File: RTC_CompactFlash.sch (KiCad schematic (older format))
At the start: 23 parts

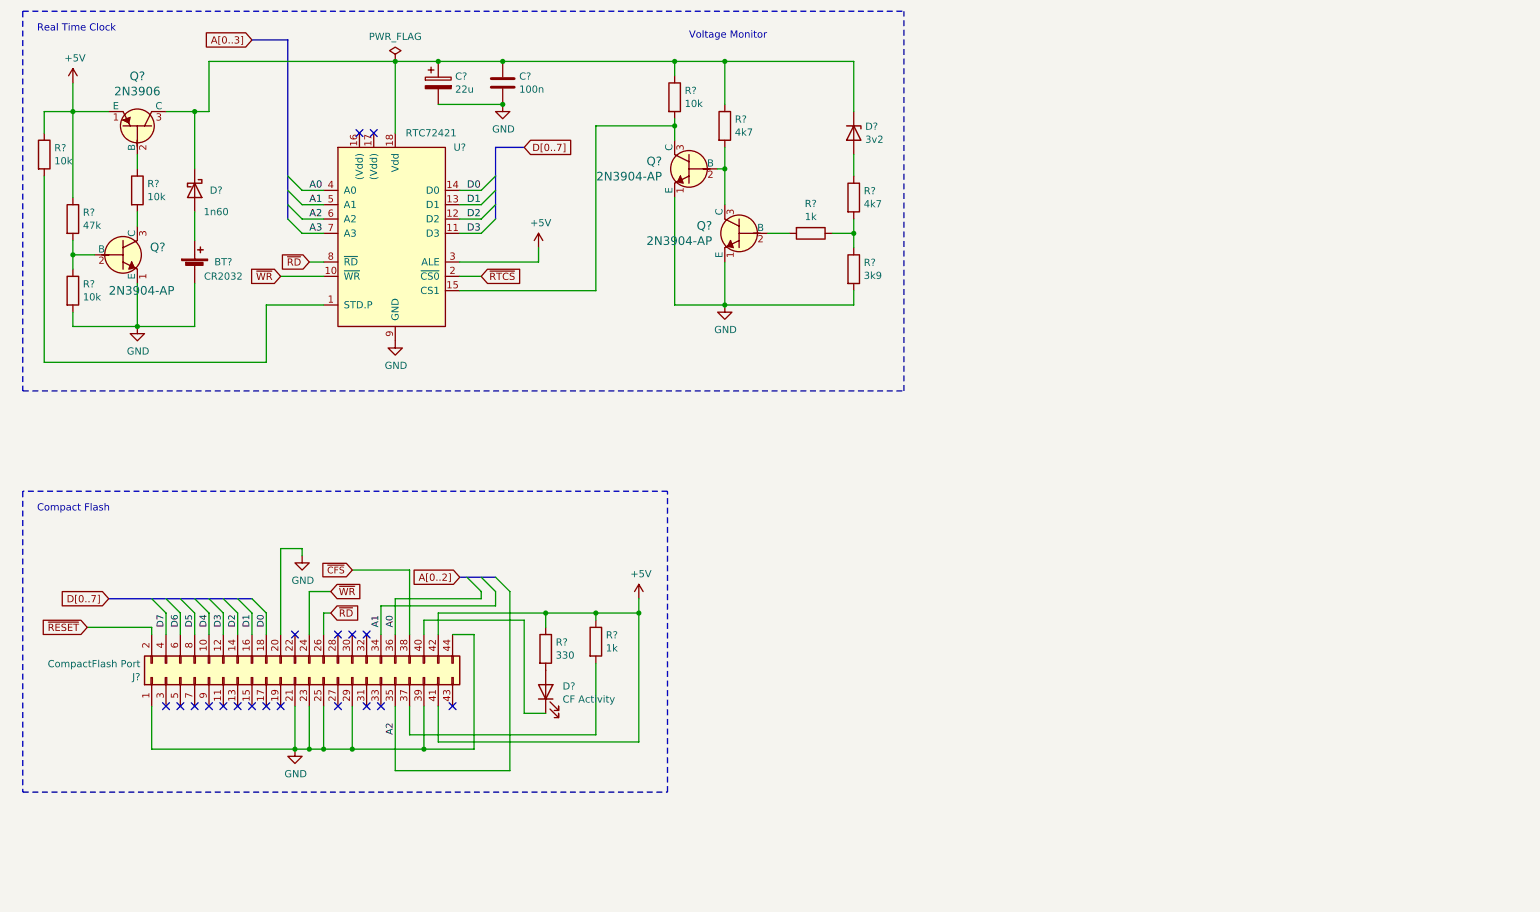
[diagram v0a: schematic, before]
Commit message: Added RTC voltage detection circuit
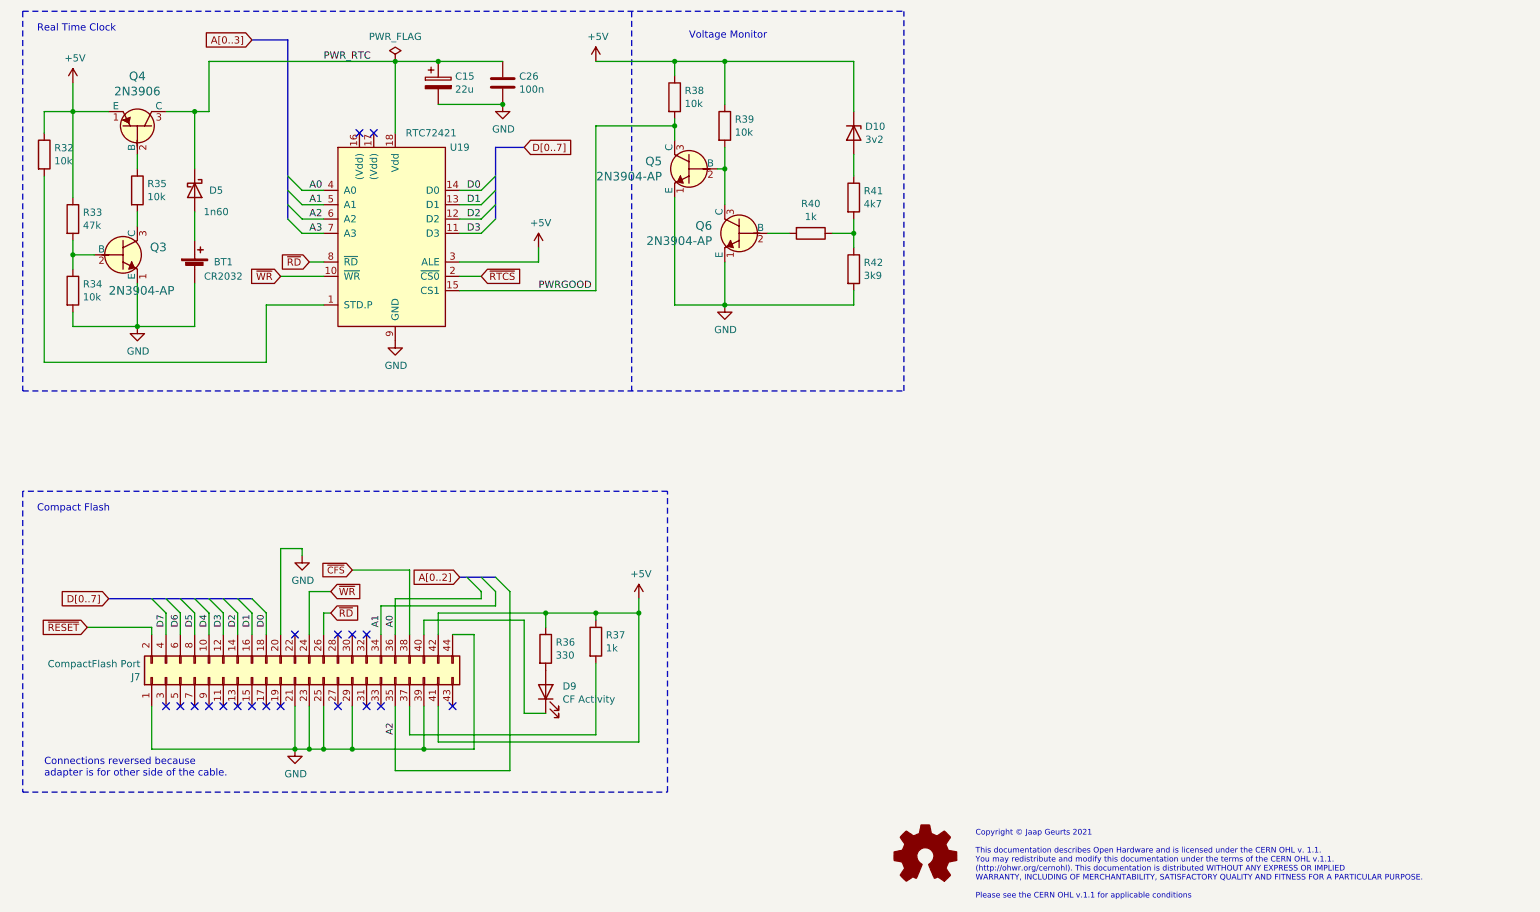
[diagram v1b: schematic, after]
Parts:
- R39: renamed from R?; value 4k7 -> 10k
- gave numbers to parts that had none: 22
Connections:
- net +5V: now also D10.1 (K), R38.1, R39.1
- net PWRGOOD: now reaches Q5.3 (C), R38.2, U19.15 (CS1)
- net PWR_RTC: now reaches C15.1, C26.1, D5.1 (K), Q4.3 (C), U19.18 (Vdd)
- net PWR_RTC: no longer D10.1 (K), R38.1, R39.1
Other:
- note added: "Connections reversed because\nadapter is for other side of the cable."
- note added: "Copyright © Jaap Geurts 2021\n\nThis documentation describes Open Hardware and is licensed under the CERN OHL v. 1.1.\nYou may redistribute and modify this documentation under the terms of the CERN OHL v.1.1.\n(http://ohwr.org/cernohl). This documentation is distributed WITHOUT ANY EXPRESS OR IMPLIED\nWARRANTY, INCLUDING OF MERCHANTABILITY, SATISFACTORY QUALITY AND FITNESS FOR A PARTICULAR PURPOS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"
